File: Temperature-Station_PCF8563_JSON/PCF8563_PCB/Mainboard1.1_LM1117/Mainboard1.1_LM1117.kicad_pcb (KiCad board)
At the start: 2 copper layers, 30 parts, among them J1 CONN_01X03, J2 CONN_01X15, J3 CONN_01X15, J4 SD_Card, J5 CONN_01X03, J6 CONN_01X02, J7 CONN_01X02, U1 LM1117-3.3, U2 PCF8563, Y1 Crystal

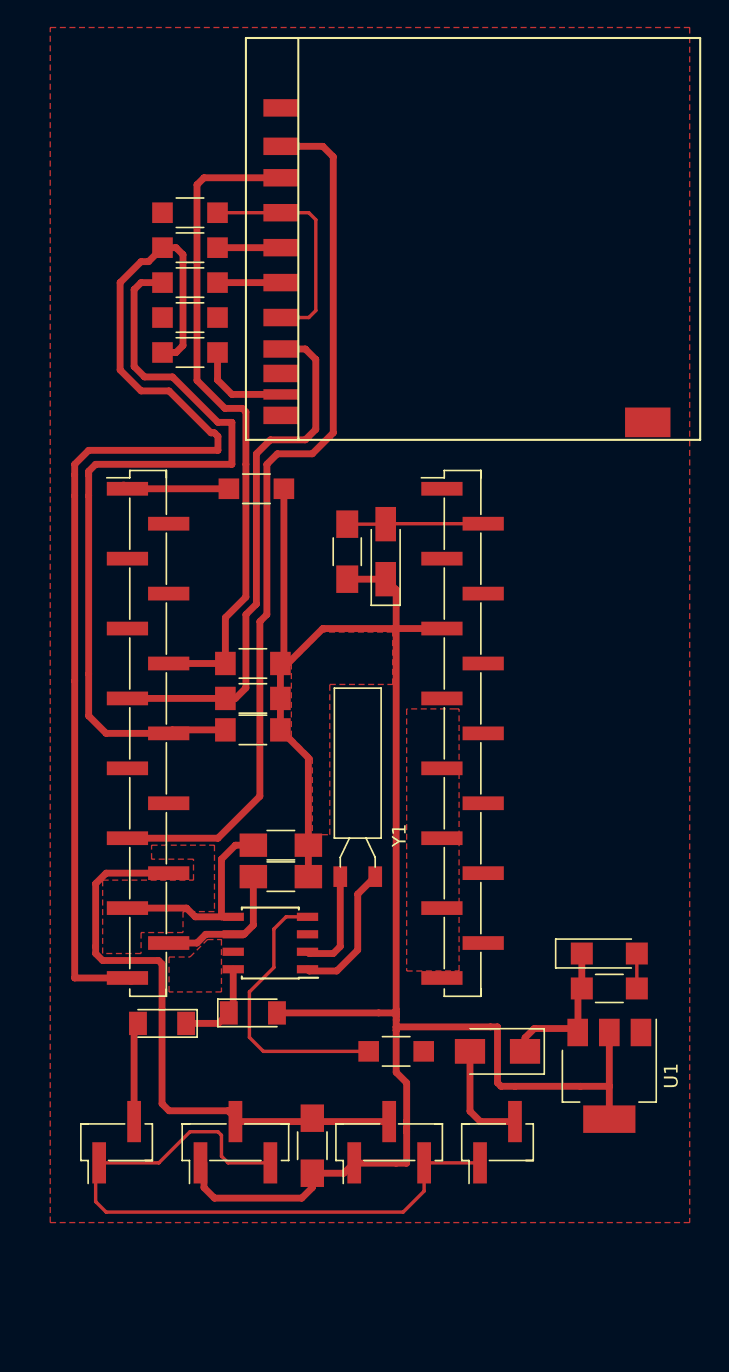
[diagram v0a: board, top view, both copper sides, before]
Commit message: Updates
Updated both versions
Added online updater
Minor cosmetic changes
Saving DHCP settings restored
Added authentication (still no HTTPS/TLS/SSL tho)
Moved as many Strings as possible to Flash memory to free RAM

Czas library:
Optimized for porting between DS3231 and PCF8563 versions.
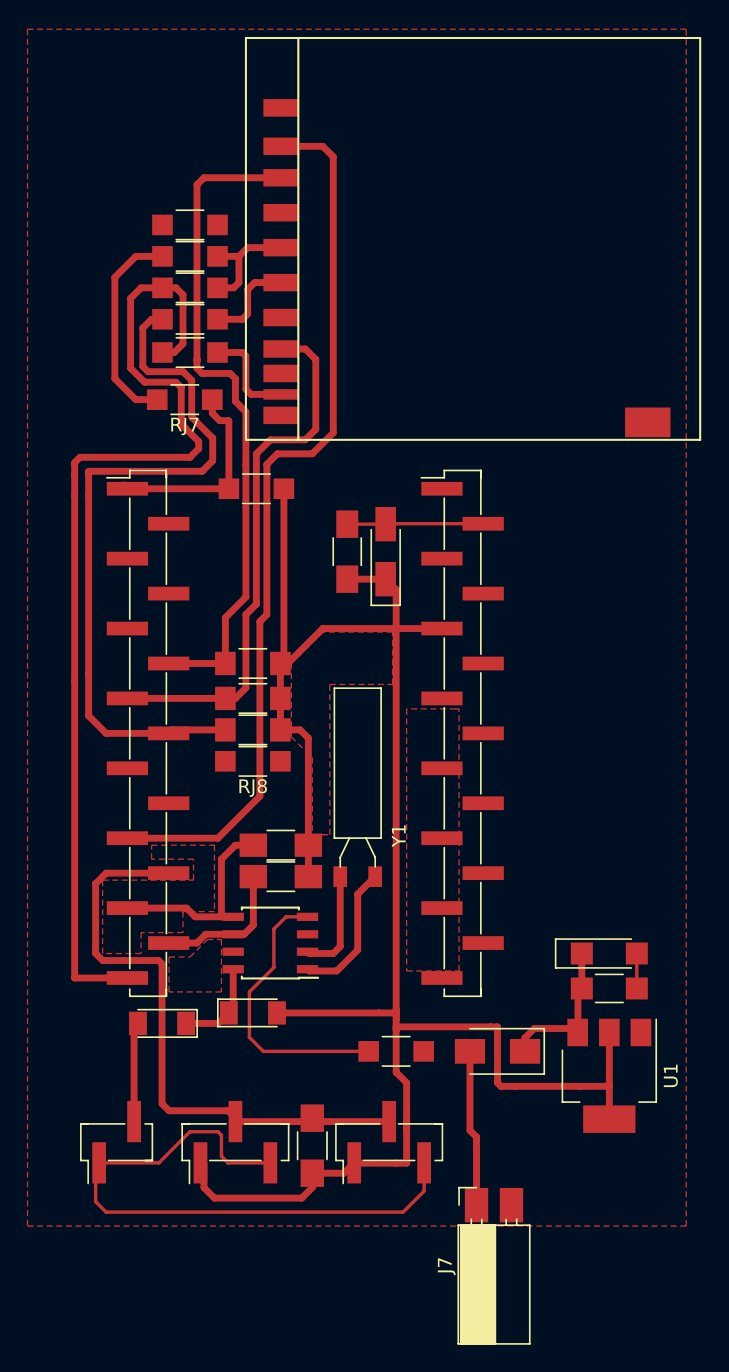
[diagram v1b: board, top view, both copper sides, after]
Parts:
- added RJ7: 0, Resistors_SMD:R_1206_HandSoldering, F.Cu at (139.8, 79.9)
- added RJ8: 0, Resistors_SMD:R_1206_HandSoldering, F.Cu at (144.8, 106.2)
- J7: footprint Pin_Headers:Pin_Header_Straight_1x02_Pitch2.54mm_SMD_Pin1Left -> Socket_Strips:Socket_Strip_Angled_1x02_Pitch2.54mm
- moved J7 4.82 mm to (161.0, 138.4)
- moved RJ3 4.45 mm to (140.2, 69.5)
- moved R4 2.92 mm to (140.2, 71.8)
- moved RJ1 2.67 mm to (140.2, 74.0)
- moved RJ4 0.89 mm to (140.2, 67.2)
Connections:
- J2 pad 10: (no net) -> Net-(J2-Pad10)
- J2 pad 3: (no net) -> Net-(J2-Pad3)
- J2 pad 4: (no net) -> Net-(J2-Pad4)
- J2 pad 5: (no net) -> Net-(J2-Pad5)
- J3 pad 1: (no net) -> Net-(J3-Pad1)
- J3 pad 10: (no net) -> Net-(J3-Pad10)
- J3 pad 11: (no net) -> Net-(J3-Pad11)
- J3 pad 12: (no net) -> Net-(J3-Pad12)
- J3 pad 13: (no net) -> Net-(J3-Pad13)
- J3 pad 14: (no net) -> Net-(J3-Pad14)
- J3 pad 15: (no net) -> Net-(J3-Pad15)
- J3 pad 3: (no net) -> Net-(J3-Pad3)
- J3 pad 4: (no net) -> Net-(J3-Pad4)
- J3 pad 7: (no net) -> Net-(J3-Pad7)
- J3 pad 8: (no net) -> Net-(J3-Pad8)
- J3 pad 9: (no net) -> Net-(J3-Pad9)
- J4 pad 11: (no net) -> Net-(J4-Pad11)
- J4 pad 8: (no net) -> Net-(J4-Pad8)
- J4 pad 9: (no net) -> Net-(J4-Pad9)
- J7 pad 1: GND -> Net-(D2-Pad2)
- J7 pad 2: Net-(D2-Pad2) -> GND
- U2 pad 3: (no net) -> Net-(U2-Pad3)
- U2 pad 7: (no net) -> Net-(U2-Pad7)
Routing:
- net 3V3: track 155.7 -> 183.3 mm
- net GND: track 99.7 -> 78.9 mm
- net SD_D: track 83.0 -> 75.1 mm
- net Net-(J2-Pad8): track 58.7 -> 52.6 mm
- net Net-(D2-Pad2): track 7.93 -> 11.1 mm
- net SCK: track 4.60 -> 6.75 mm
- net MOSI: track 48.1 -> 48.6 mm
